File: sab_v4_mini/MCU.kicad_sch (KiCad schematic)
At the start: 44 parts, among them J5 USB_C_Receptacle_USB2.0, SW1 SW_SPST, U1 IS42S16100H-7TL, U16 USBLC6-2P6, U17 W25Q128JVS, U19 FE1.1s, U7 STM32H723ZGTx, Y2 X1E0000210132, Y3 Crystal_GND24

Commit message: deleted unused pin added mcu
stm32h750vbt6
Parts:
- removed R2: 10k, Resistor_SMD:R_0603_1608Metric, symbol Device:R
- removed U1: IS42S16100H-7TL, Library:TSOP-2-50-new, symbol stm_audio:IS42S16100H-7TL
- removed U17: W25Q128JVS, Package_SO:SOIC-8_5.23x5.23mm_P1.27mm, symbol Memory_Flash:W25Q128JVS
- removed U19: FE1.1s, Package_SO:SSOP-28_3.9x9.9mm_P0.635mm, symbol Interface_USB:FE1.1s
- removed U7: STM32H723ZGTx, Package_QFP:LQFP-144_20x20mm_P0.5mm, symbol MCU_ST_STM32H7:STM32H723ZGTx
- added J6: BOOT0_Conn_01x03, symbol Connector_Generic:Conn_01x03
- added R12: 10k, Resistor_SMD:R_0603_1608Metric, symbol Device:R
- added U7: STM32H750VBTx, Package_QFP:LQFP-100_14x14mm_P0.5mm, symbol MCU_ST_STM32H7:STM32H750VBTx
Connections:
- net +3.3V: now also J6.3 (Pin_3), U7.100 (VDD), U7.11 (VDD), U7.20 (VREF+), U7.21 (VDDA), U7.27 (VDD), U7.50 (VDD), U7.6 (VBAT), U7.75 (VDD)
- net DSP_USB_HS_D+: now also U16.6 (I/O1)
- net DSP_USB_HS_D-: now also U16.4 (I/O2)
- net GND: now also J6.1 (Pin_1), U7.10 (VSS), U7.19 (VSSA), U7.26 (VSS), U7.49 (VSS), U7.74 (VSS), U7.99 (VSS)
- net NRST: now also U7.14 (NRST)
- net OSC0: now also U7.12 (PH0)
- net OSC1: now also U7.13 (PH1)
- net DSP_VBUS: now reaches C12.1, J5.A4 (VBUS), J5.A9 (VBUS), J5.B4 (VBUS), J5.B9 (VBUS)
- net at C15.1: now also U7.48 (VCAP)
- net at C15.1: now also U7.73 (VCAP)
- new net: J6.2 (Pin_2), R12.2
- new net to_BOOT0: R12.1, U7.94 (BOOT0)
- no-connect marks 4 -> 0
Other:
- note added: "BOOT pin"
- note removed: "SDRAM"
- moved on the sheet: C12, C15

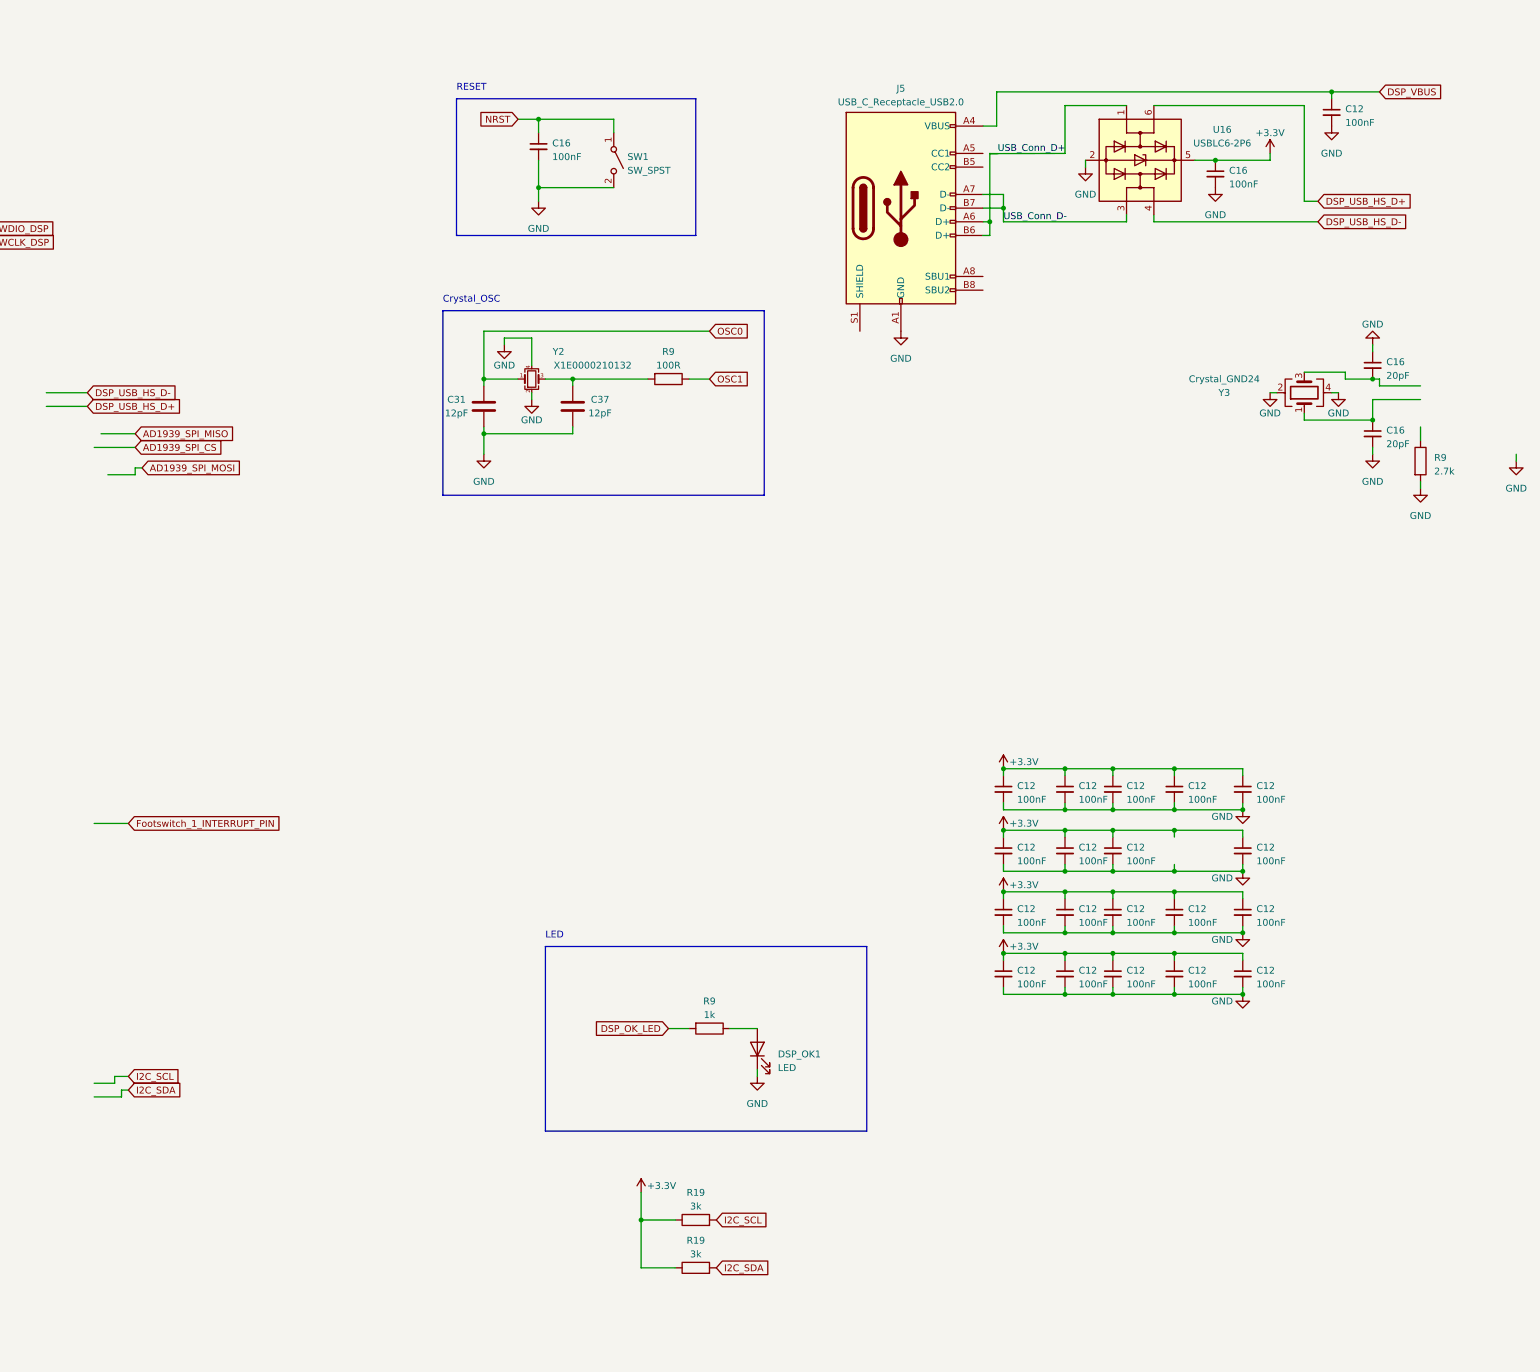
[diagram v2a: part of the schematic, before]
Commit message: added codec
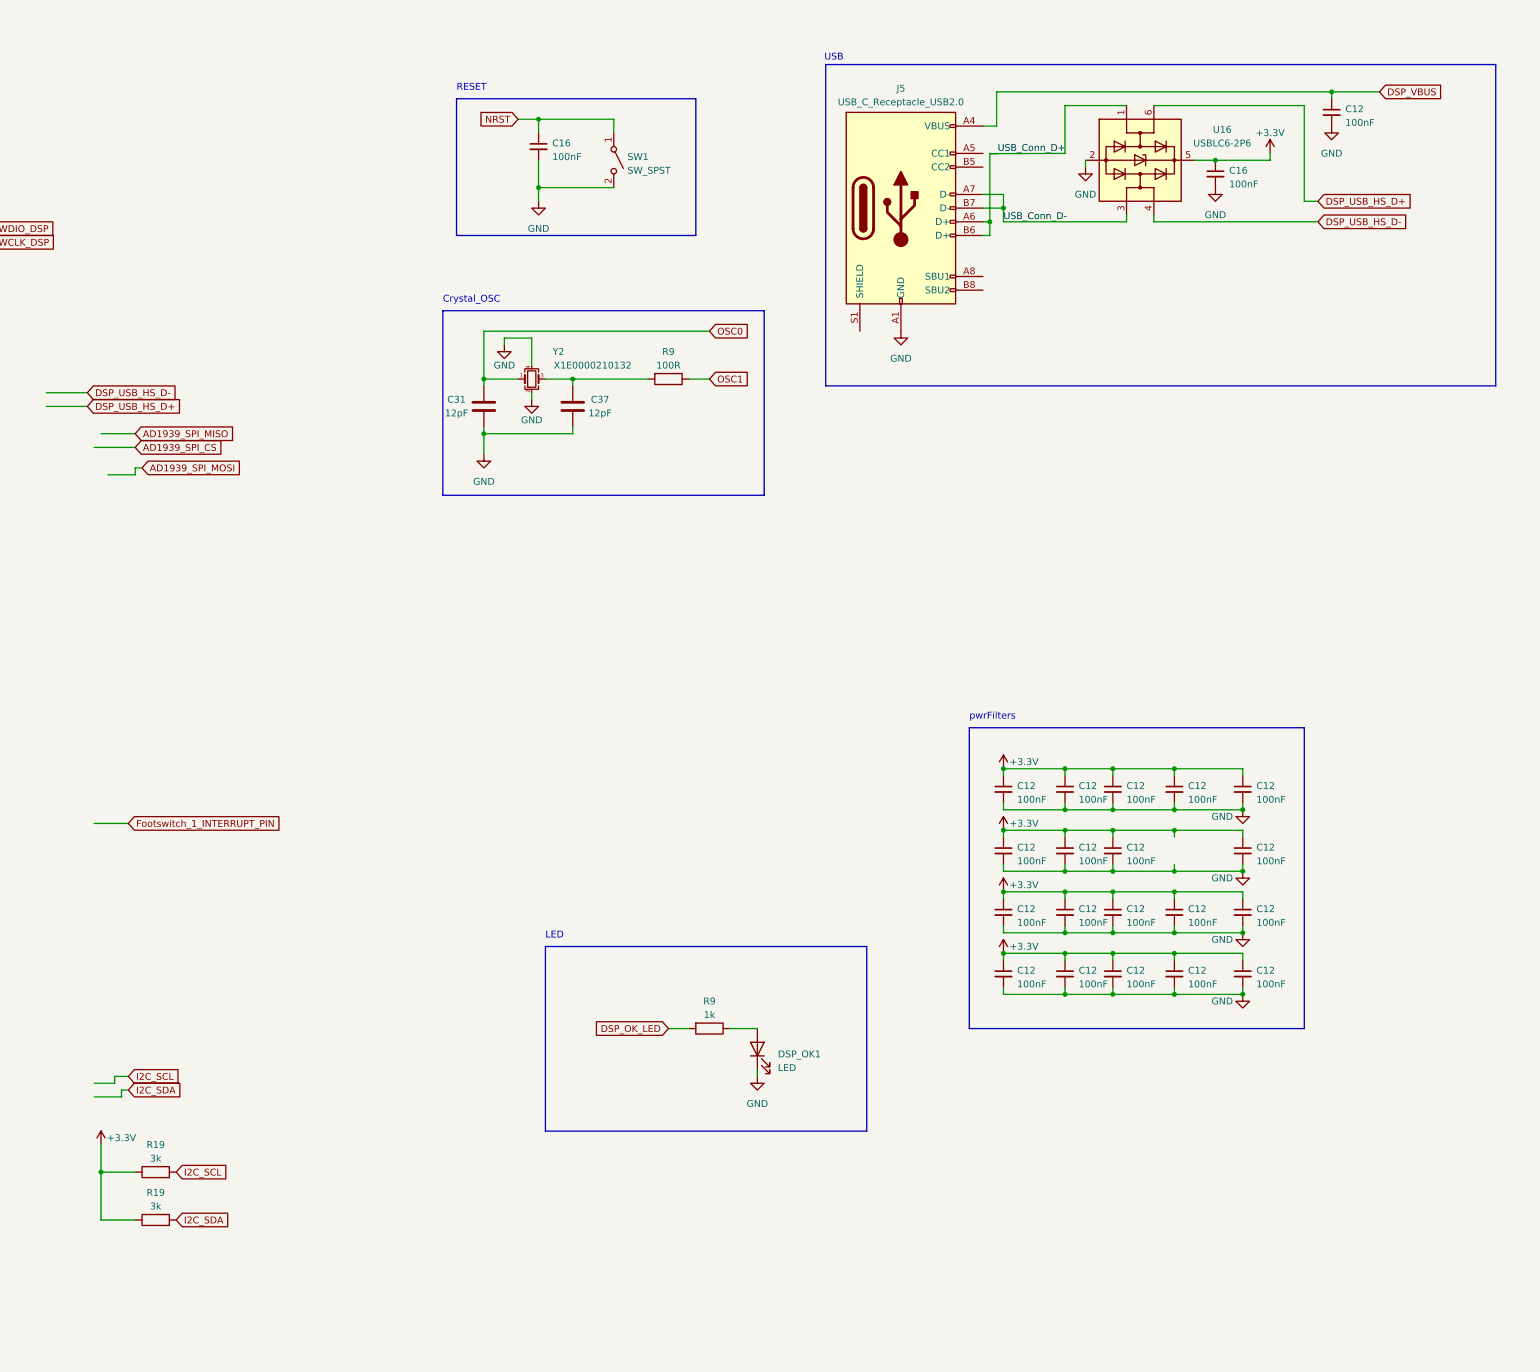
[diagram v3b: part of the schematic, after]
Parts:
- removed C16 (x2): 20pF, Capacitor_SMD:C_0402_1005Metric, symbol Device:C_Small
- removed R9: 2.7k, Resistor_SMD:R_0603_1608Metric, symbol Device:R
- removed Y3: Crystal_GND24, Crystal:Crystal_SMD_3225-4Pin_3.2x2.5mm, symbol Device:Crystal_GND24
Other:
- note added: "USB"
- note added: "pwrFilters"
- moved on the sheet: R19
